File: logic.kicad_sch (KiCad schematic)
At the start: 48 parts

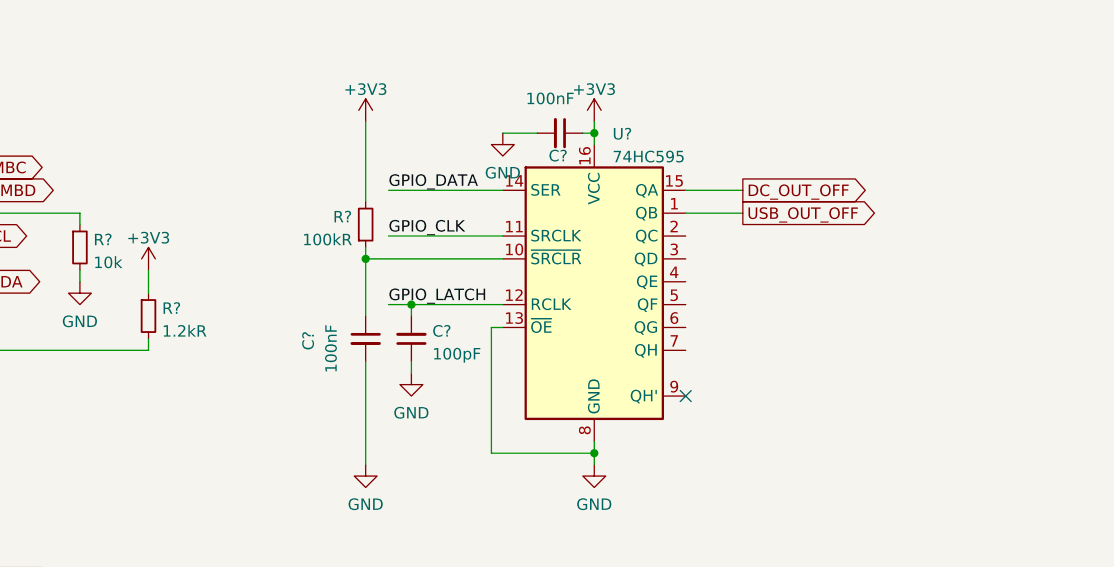
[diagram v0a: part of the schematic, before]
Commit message: Add partial DC output circuitry
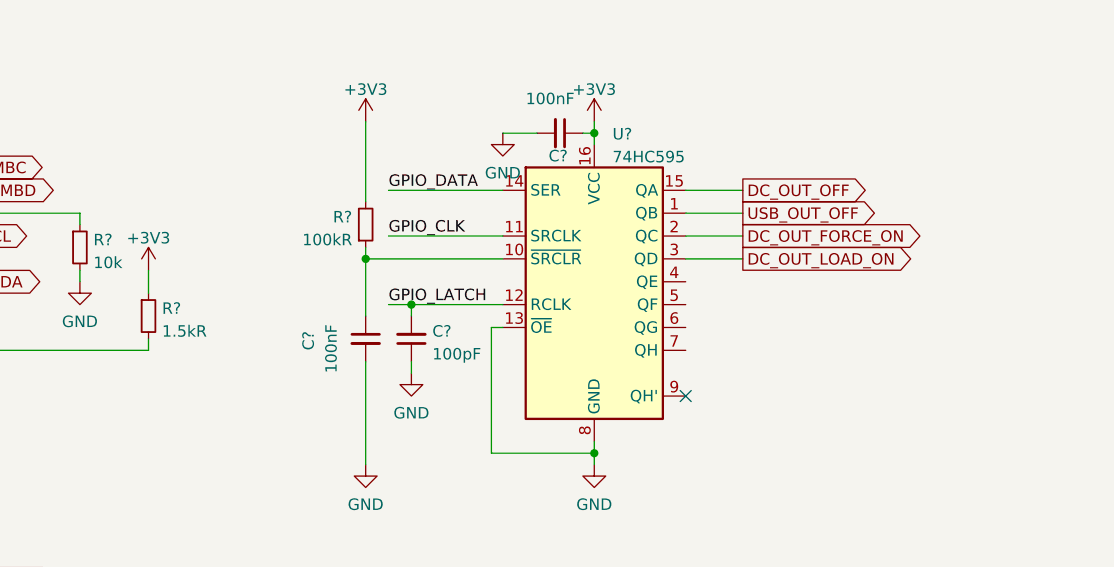
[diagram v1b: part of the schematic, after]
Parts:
- R?: value 1.2kR -> 1.5kR; LCSC C25862 -> C25867
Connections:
- net DC_OUT_FORCE_ON: now reaches U?.2 (QC)
- net DC_OUT_LOAD_ON: now reaches U?.3 (QD)
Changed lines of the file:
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@@
+    (stroke (width 0) (type default) (color 0 0 0 0))
+  )
+  (wire (pts (xy 167.64 140.97) (xy 173.99 140.97))
     (stroke (width 0) (type default) (color 0 0 0 0))
   )
@@
   )
   (wire (pts (xy 25.4 111.76) (xy 25.4 114.3))
+    (stroke (width 0) (type default) (color 0 0 0 0))
+  )
+  (wire (pts (xy 167.64 143.51) (xy 173.99 143.51))
     (stroke (width 0) (type default) (color 0 0 0 0))
   )
@@
   (label "MDC" (at 114.3 74.93 0)
     (effects (font (size 1.27 1.27)) (justify left bottom))
+  )
+  (global_label "DC_OUT_LOAD_ON" (shape output) (at 173.99 143.51 0) (fields_autoplaced)
+    (effects (font (size 1.27 1.27)) (justify left))
+    (property "Referenzen zwischen Schaltplänen" "${INTERSHEET_REFS}" (id 0) (at 192.8526 143.4306 0)
+      (effects (font (size 1.27 1.27)) (justify left) hide)
+    )
   )
   (global_label "SDA" (shape bidirectional) (at 88.9 146.05 0) (fields_autoplaced)
     (effects (font (size 1.27 1.27)) (justify left))
     (property "Referenzen zwischen Schaltplänen" "${INTERSHEET_REFS}" (id 0) (at 94.8812 145.9706 0)
+      (effects (font (size 1.27 1.27)) (justify left) hide)
+    )
+  )
+  (global_label "DC_OUT_FORCE_ON" (shape output) (at 173.99 140.97 0) (fields_autoplaced)
+    (effects (font (size 1.27 1.27)) (justify left))
+    (property "Referenzen zwischen Schaltplänen" "${INTERSHEET_REFS}" (id 0) (at 194.2436 140.8906 0)
       (effects (font (size 1.27 1.27)) (justify left) hide)
     )
@@
       (effects (font (size 1.27 1.27)) (justify left))
     )
-    (property "Value" "1.2kR" (id 1) (at 109.4486 151.5622 0)
+    (property "Value" "1.5kR" (id 1) (at 109.4486 151.5622 0)
       (effects (font (size 1.27 1.27)) (justify left))
     )
@@
       (effects (font (size 1.27 1.27)) hide)
     )
-    (property "LCSC" "C25862" (id 4) (at 107.95 149.86 0)
-      (effects (font (size 1.27 1.27)) hide)
-    )
+    (property "LCSC" "C25867" (id 4) (at 107.95 149.86 0)
+      (effects (font (size 1.27 1.27)) hide)
+    )

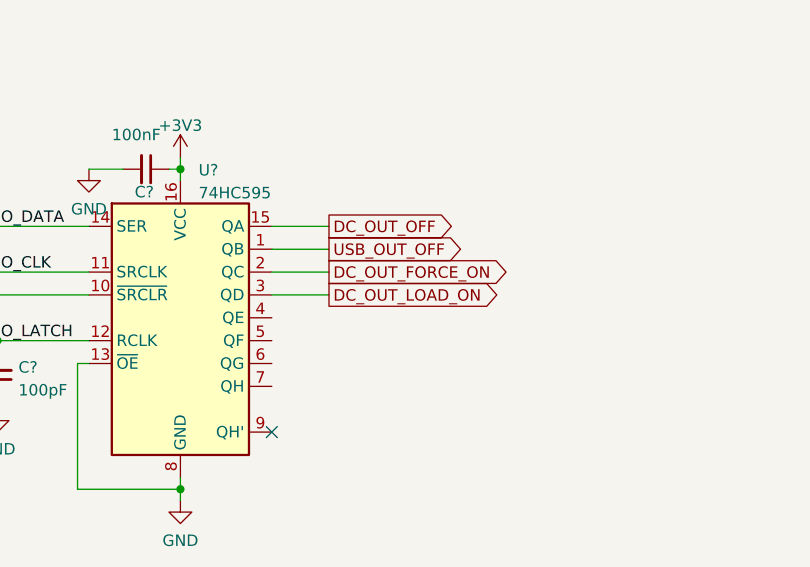
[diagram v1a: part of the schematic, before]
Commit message: Finish DC output schematic capture
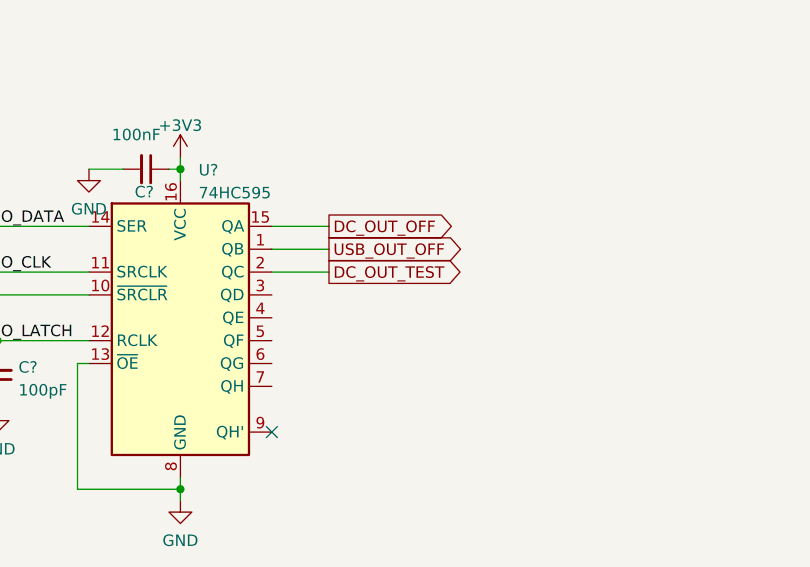
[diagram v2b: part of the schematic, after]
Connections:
- net DC_OUT_FORCE_ON renamed DC_OUT_TEST
- net DC_OUT_LOAD_ON: no longer names the net of U?.3 (QD)
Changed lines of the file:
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@@
-    (stroke (width 0) (type default) (color 0 0 0 0))
-  )
-  (wire (pts (xy 167.64 143.51) (xy 173.99 143.51))
     (stroke (width 0) (type default) (color 0 0 0 0))
   )
@@
   (label "MDC" (at 114.3 74.93 0)
     (effects (font (size 1.27 1.27)) (justify left bottom))
-  )
-  (global_label "DC_OUT_LOAD_ON" (shape output) (at 173.99 143.51 0) (fields_autoplaced)
-    (effects (font (size 1.27 1.27)) (justify left))
-    (property "Referenzen zwischen Schaltplänen" "${INTERSHEET_REFS}" (id 0) (at 192.8526 143.4306 0)
-      (effects (font (size 1.27 1.27)) (justify left) hide)
-    )
   )
   (global_label "SDA" (shape bidirectional) (at 88.9 146.05 0) (fields_autoplaced)
@@
     )
   )
-  (global_label "DC_OUT_FORCE_ON" (shape output) (at 173.99 140.97 0) (fields_autoplaced)
+  (global_label "DC_OUT_TEST" (shape output) (at 173.99 140.97 0) (fields_autoplaced)
     (effects (font (size 1.27 1.27)) (justify left))
-    (property "Referenzen zwischen Schaltplänen" "${INTERSHEET_REFS}" (id 0) (at 194.2436 140.8906 0)
+    (property "Referenzen zwischen Schaltplänen" "${INTERSHEET_REFS}" (id 0) (at 188.8007 140.8906 0)
       (effects (font (size 1.27 1.27)) (justify left) hide)
     )

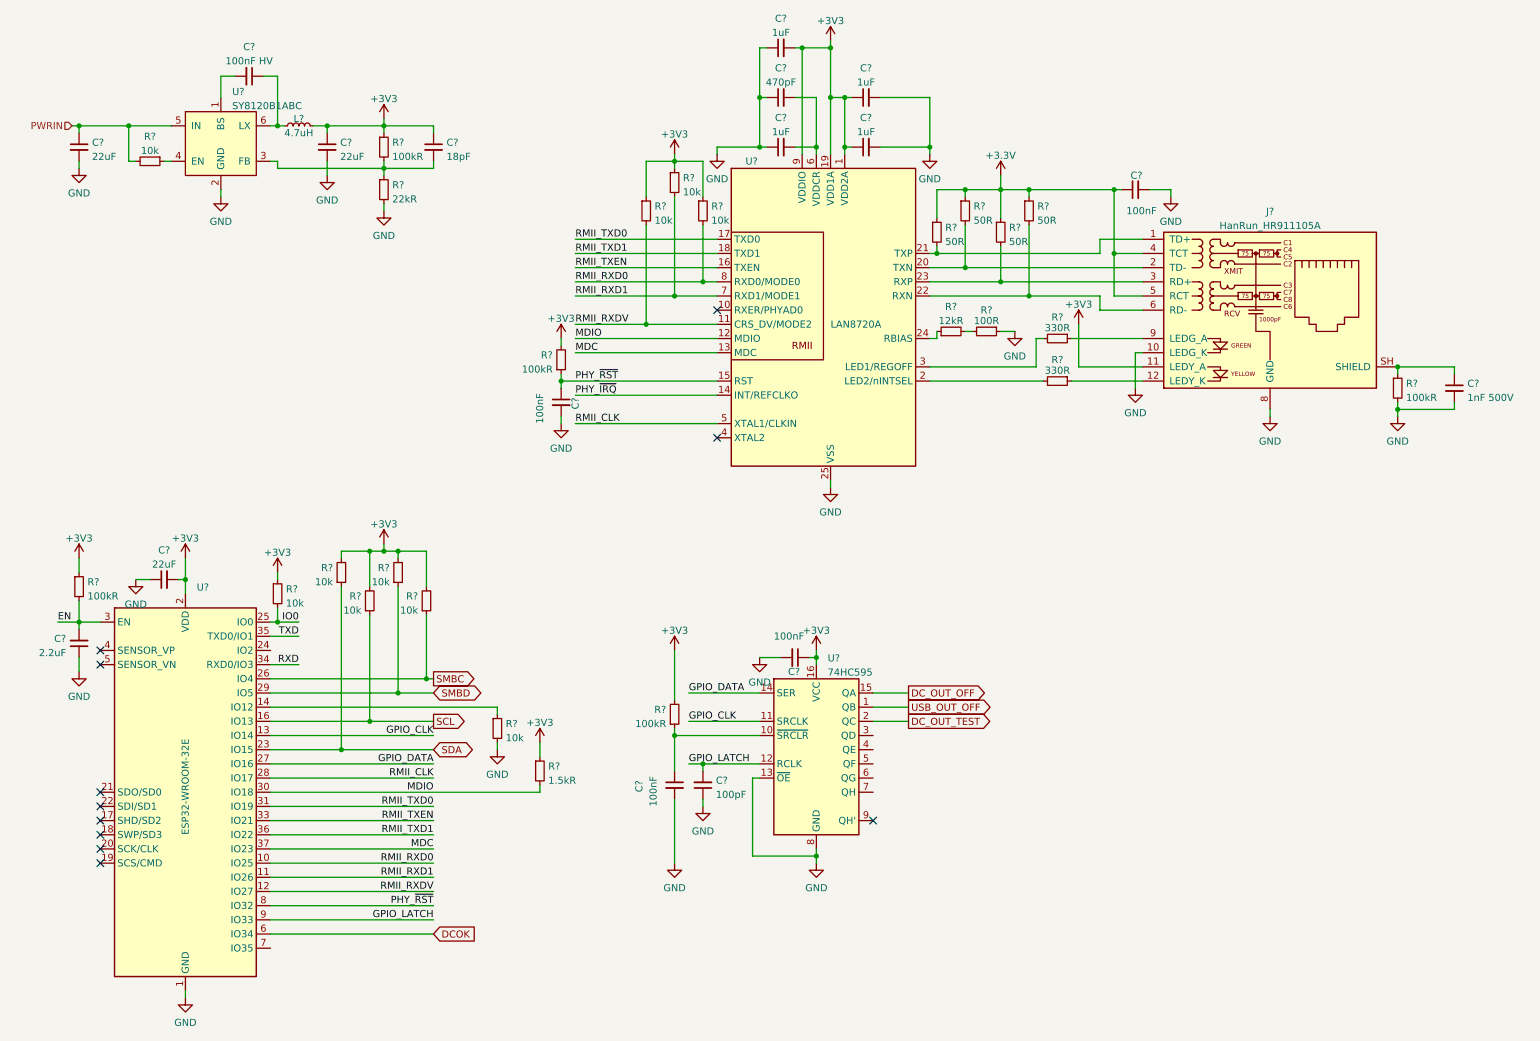
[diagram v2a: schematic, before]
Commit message: Add barrel jack footprints
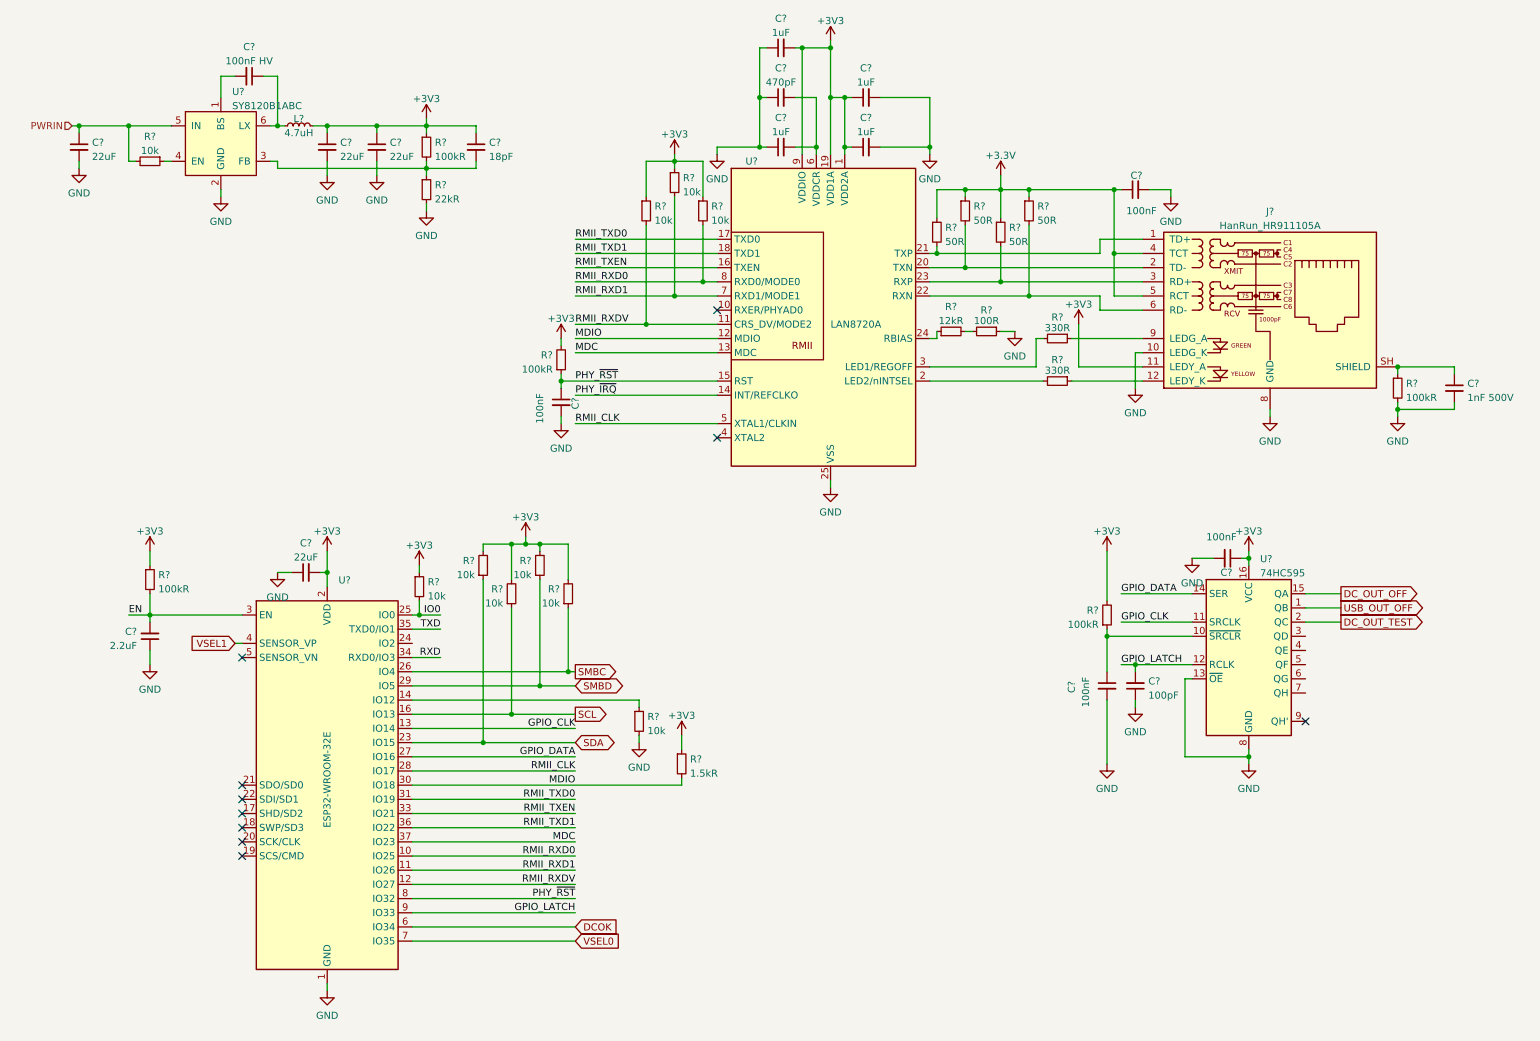
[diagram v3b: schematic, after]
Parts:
- added C?: 22uF, Capacitor_SMD:C_0805_2012Metric, symbol Device:C_Small
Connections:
- net +3V3: now also C?.1
- net GND: now also C?.2
- net VSEL1: now reaches U?.4 (SENSOR_VP)
- net VSEL0: now reaches U?.7 (IO35)
- no-connect marks 11 -> 10
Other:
- moved on the sheet: C?, R?, U?

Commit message: Add individually switchable outputs
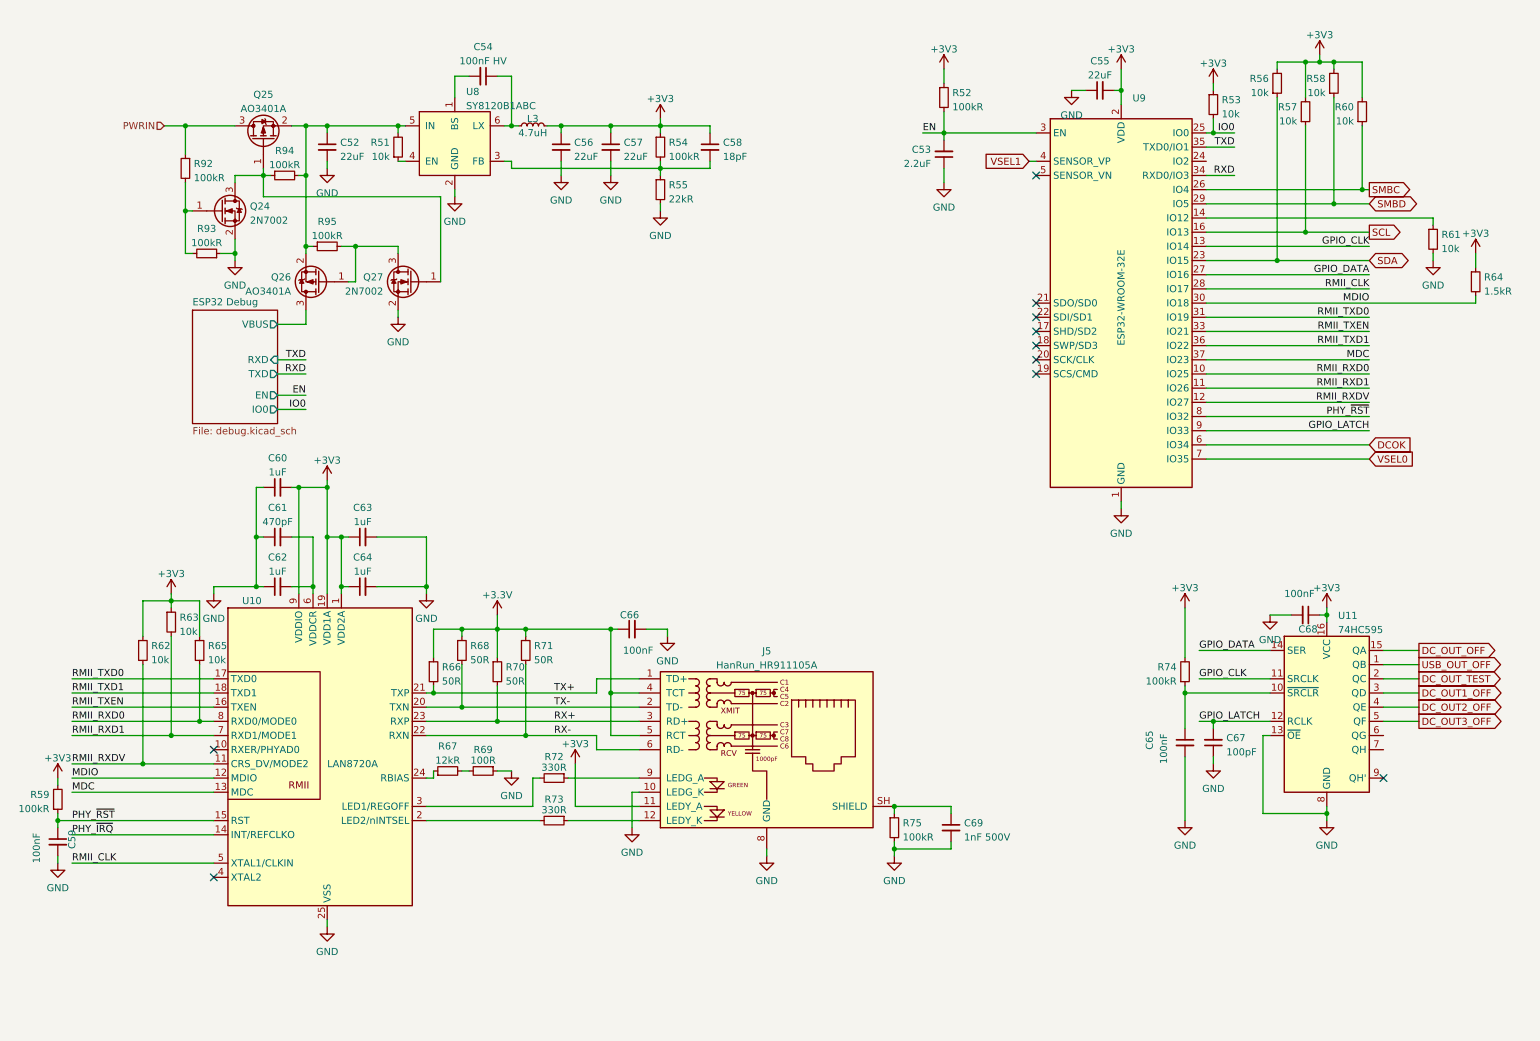
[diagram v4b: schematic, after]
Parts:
- added Q24, Q27: 2N7002, Package_TO_SOT_SMD:SOT-23, symbol Transistor_FET:2N7002
- added Q25, Q26: AO3401A, Package_TO_SOT_SMD:SOT-23, symbol Transistor_FET:AO3401A
- added R92, R93, R94, R95: 100kR, Resistor_SMD:R_0402_1005Metric, symbol Device:R_Small
- gave numbers to parts that had none: 49
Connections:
- net GND: now also Q24.2 (S), Q27.2 (S), R93.1
- net PWRIN: now also Q25.3 (D), R92.1; no longer C52.1, R51.2, U8.5 (IN)
- net TX-: now reaches J5.2 (TD-), R68.2, U10.20 (TXN)
- net TX+: now reaches J5.1 (TD+), R66.2, U10.21 (TXP)
- net RX-: now reaches J5.6 (RD-), R71.2, U10.22 (RXN)
- net RX+: now reaches J5.3 (RD+), R70.2, U10.23 (RXP)
- net DC_OUT1_OFF: now reaches U11.3 (QD)
- net DC_OUT2_OFF: now reaches U11.4 (QE)
- net DC_OUT3_OFF: now reaches U11.5 (QF)
- new net: Q24.3 (D), Q25.1 (G), Q27.1 (G), R94.1
- new net: C52.1, Q25.2 (S), Q26.2 (S), R51.2, R94.2, R95.1, U8.5 (IN)
- new net: Q26.1 (G), Q27.3 (D), R95.2
- new net: Q24.1 (G), R92.2, R93.2
- new net ESP32 Debug/VBUS: Q26.3 (D)
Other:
- added sheet ESP32 Debug (debug.kicad_sch)
- moved on the sheet: C52, C53, C54, C55, C56, C57, C58, C59, C60, C61, C62, C63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
